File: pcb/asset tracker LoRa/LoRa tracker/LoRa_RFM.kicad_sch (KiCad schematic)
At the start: 2 parts

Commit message: pcb kastje
pcb in kastje getekend
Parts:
- removed MOD1: rfm95, Module:RFM69HW, symbol modulles:rfm95
- added C25: 10uF, vanalles:0603, symbol Device:C_Small
- added C26: 1uF, vanalles:0603, symbol Device:C_Small
- added C27: 0.1uF, vanalles:0603, symbol Device:C_Small
- added C32: 100nF, vanalles:0603, symbol Device:C_Small
- added CON3: jtag, connectors_user:Tag-Connect_TC2050-IDC-FP_2x05_P1.27mm_Vertical, symbol conectors:jtag
- added R9: 10K, vanalles:0603RL, symbol Device:R_Small_US
- added U8: murattaLora, Module:XCVR_CMWX1ZZABZ-078, symbol modulles:murattaLora
- R7: footprint vanalles:0603 -> vanalles:0603RL
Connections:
- net +3V3: now also C25.1, C26.1, C27.1, CON3.1 (VCC), R9.1, U8.32 (VREF+), U8.5 (VDD_MCU), U8.6 (VDD_RF); no longer R7.1
- net GND: now also R7.1, C25.2, C26.2, C27.2, C32.2, CON3.3 (GND), CON3.5 (GND), CON3.9 (GND), U8.25 (GND), U8.27 (GND), U8.3 (GND), U8.44 (GND), U8.49 (GND), U8.50 (GND), U8.51 (GND), U8.52 (GND), U8.53 (GND), U8.54 (GND), U8.55 (GND), U8.56 (GND), U8.57 (GND), U8.7 (GND)
- net CS_RFM: no longer names the net of R7.2
- net CS_RFM: now also U8.43 (BOOT0)
- new net ANT: U8.26 (ANT)
- new net CLK: U8.16 (PB13/SPI2_SCK)
- new net CS: U8.17 (PB12/SPI2_NSS)
- new net MISO: U8.15 (PB14/SPI2_MISO)
- new net MOSI: U8.14 (PB15/SPI2_MOSI)
- new net RESET: C32.1, CON3.10 (tRST), R9.2, U8.34 (MCU_NRST)
- new net SWCLK: CON3.4 (SWDCLK/TCK), U8.42 (PA14/SWCLK)
- new net SWDIO: CON3.2 (SWDIO/TMS), U8.41 (PA13/SWDIO)

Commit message: klaar
print hertekend naar stm32L5
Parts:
- added R10: 10K, vanalles:0603RL, symbol Device:R_Small_US
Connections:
- net +3V3: now also R10.1
- net CS: now also R10.2
- no-connect marks 5 -> 32
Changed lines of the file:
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@@
   (junction (at 171.45 33.02) (diameter 0.9144) (color 0 0 0 0))
   (junction (at 171.45 35.56) (diameter 0.9144) (color 0 0 0 0))
+  (junction (at 172.72 73.66) (diameter 0.9144) (color 0 0 0 0))
   (junction (at 189.23 31.75) (diameter 0.9144) (color 0 0 0 0))
   (junction (at 198.12 135.89) (diameter 0.9144) (color 0 0 0 0))
@@
   (junction (at 270.51 135.89) (diameter 0.9144) (color 0 0 0 0))
   (no_connect (at 100.33 33.02))
+  (no_connect (at 100.33 43.18))
+  (no_connect (at 100.33 45.72))
+  (no_connect (at 100.33 48.26))
+  (no_connect (at 100.33 50.8))
+  (no_connect (at 100.33 53.34))
+  (no_connect (at 100.33 55.88))
+  (no_connect (at 100.33 60.96))
+  (no_connect (at 100.33 63.5))
+  (no_connect (at 100.33 66.04))
+  (no_connect (at 100.33 68.58))
+  (no_connect (at 100.33 71.12))
+  (no_connect (at 100.33 73.66))
+  (no_connect (at 100.33 76.2))
+  (no_connect (at 100.33 78.74))
+  (no_connect (at 100.33 81.28))
+  (no_connect (at 100.33 83.82))
+  (no_connect (at 100.33 99.06))
+  (no_connect (at 100.33 101.6))
+  (no_connect (at 100.33 104.14))
+  (no_connect (at 100.33 109.22))
+  (no_connect (at 100.33 111.76))
   (no_connect (at 156.21 30.48))
   (no_connect (at 156.21 40.64))
+  (no_connect (at 156.21 58.42))
+  (no_connect (at 156.21 60.96))
+  (no_connect (at 156.21 63.5))
+  (no_connect (at 156.21 66.04))
+  (no_connect (at 156.21 68.58))
+  (no_connect (at 156.21 72.39))
   (no_connect (at 228.6 130.81))
   (no_connect (at 228.6 133.35))
@@
     (stroke (width 0) (type solid) (color 0 0 0 0))
   )
-  (wire (pts (xy 156.21 76.2) (xy 172.72 76.2))
-    (stroke (width 0) (type solid) (color 0 0 0 0))
-  )
-  (wire (pts (xy 156.21 78.74) (xy 172.72 78.74))
-    (stroke (width 0) (type solid) (color 0 0 0 0))
-  )
-  (wire (pts (xy 156.21 81.28) (xy 172.72 81.28))
+  (wire (pts (xy 156.21 76.2) (xy 191.77 76.2))
+    (stroke (width 0) (type solid) (color 0 0 0 0))
+  )
+  (wire (pts (xy 156.21 78.74) (xy 191.77 78.74))
+    (stroke (width 0) (type solid) (color 0 0 0 0))
+  )
+  (wire (pts (xy 156.21 81.28) (xy 191.77 81.28))
     (stroke (width 0) (type solid) (color 0 0 0 0))
   )
@@
   )
   (wire (pts (xy 171.45 35.56) (xy 171.45 38.1))
+    (stroke (width 0) (type solid) (color 0 0 0 0))
+  )
+  (wire (pts (xy 172.72 55.88) (xy 172.72 62.23))
+    (stroke (width 0) (type solid) (color 0 0 0 0))
+  )
+  (wire (pts (xy 172.72 67.31) (xy 172.72 73.66))
+    (stroke (width 0) (type solid) (color 0 0 0 0))
+  )
+  (wire (pts (xy 172.72 73.66) (xy 191.77 73.66))
     (stroke (width 0) (type solid) (color 0 0 0 0))
   )
@@
     (effects (font (size 1.27 1.27)) (justify right))
   )
-  (hierarchical_label "CS" (shape input) (at 172.72 73.66 0)
-    (effects (font (size 1.27 1.27)) (justify left))
-  )
-  (hierarchical_label "CLK" (shape input) (at 172.72 76.2 0)
-    (effects (font (size 1.27 1.27)) (justify left))
-  )
-  (hierarchical_label "MISO" (shape output) (at 172.72 78.74 0)
-    (effects (font (size 1.27 1.27)) (justify left))
-  )
-  (hierarchical_label "MOSI" (shape input) (at 172.72 81.28 0)
+  (hierarchical_label "CS" (shape input) (at 191.77 73.66 0)
+    (effects (font (size 1.27 1.27)) (justify left))
+  )
+  (hierarchical_label "CLK" (shape input) (at 191.77 76.2 0)
+    (effects (font (size 1.27 1.27)) (justify left))
+  )
+  (hierarchical_label "MISO" (shape output) (at 191.77 78.74 0)
+    (effects (font (size 1.27 1.27)) (justify left))
+  )
+  (hierarchical_label "MOSI" (shape input) (at 191.77 81.28 0)
     (effects (font (size 1.27 1.27)) (justify left))
   )
@@
     )
     (property "Datasheet" "" (id 3) (at 171.45 25.4 0)
+      (effects (font (size 1.27 1.27)) hide)
+    )
+    (pin "1")
+  )
+  (symbol (lib_id "power:+3V3") (at 172.72 55.88 0) (unit 1)
+    (in_bom yes) (on_board yes) (fields_autoplaced)
+    (property "Reference" "#PWR0161" (id 0) (at 172.72 59.69 0)
+      (effects (font (size 1.27 1.27)) hide)
+    )
+    (property "Value" "+3V3" (id 1) (at 172.72 52.07 0))
+    (property "Footprint" "" (id 2) (at 172.72 55.88 0)
+      (effects (font (size 1.27 1.27)) hide)
+    )
+    (property "Datasheet" "" (id 3) (at 172.72 55.88 0)
       (effects (font (size 1.27 1.27)) hide)
     )
@@
       (effects (font (size 1.27 1.27)) hide)
     )
+    (pin "1")
+    (pin "2")
+  )
+  (symbol (lib_id "Device:R_Small_US") (at 172.72 64.77 0) (unit 1)
+    (in_bom yes) (on_board yes) (fields_autoplaced)
+    (property "Reference" "R10" (id 0) (at 175.26 64.1349 0)
+      (effects (font (size 1.27 1.27)) (justify left))
+    )
+    (property "Value" "10K" (id 1) (at 175.26 66.6749 0)
+      (effects (font (size 1.27 1.27)) (justify left))
+    )
+    (property "Footprint" "vanalles:0603RL" (id 2) (at 172.72 64.77 0)
+      (effects (font (size 1.27 1.27)) hide)
+    )
+    (property "Datasheet" "~" (id 3) (at 172.72 64.77 0)
+      (effects (font (size 1.27 1.27)) hide)
+    )

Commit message: remake
remake 2 van de print
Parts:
- removed C32: 100nF, vanalles:0603, symbol Device:C_Small
- removed CON3: jtag, connectors_user:Tag-Connect_TC2050-IDC-FP_2x05_P1.27mm_Vertical, symbol conectors:jtag
- removed R10, R9: 10K, vanalles:0603RL, symbol Device:R_Small_US
- removed U8: murattaLora, Module:XCVR_CMWX1ZZABZ-078, symbol modulles:murattaLora
- added MOD1: RFM98W-433S2, Module:XCVR_RFM98W-433S2, symbol RFM98W-433S2:RFM98W-433S2
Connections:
- net +3V3: now also R7.1, MOD1.13 (3.3V), MOD1.13_1 (3.3V)
- net ANT: now also MOD1.9 (ANT), MOD1.9_1 (ANT)
- net CLK: now also MOD1.4 (SCK), MOD1.4_1 (SCK)
- net CS: now also R7.2, MOD1.5 (NSS), MOD1.5_1 (NSS)
- net GND: now also MOD1.1 (GND), MOD1.10 (GND), MOD1.10_1 (GND), MOD1.1_1 (GND), MOD1.8 (GND), MOD1.8_1 (GND); no longer R7.1
- net MISO: now also MOD1.2 (MISO), MOD1.2_1 (MISO)
- net MOSI: now also MOD1.3 (MOSI), MOD1.3_1 (MOSI)
- net RESET: now also MOD1.6 (RESET), MOD1.6_1 (RESET)
- new net: MOD1.11 (DIO3), MOD1.11_1 (DIO3)
- new net: MOD1.12 (DIO4), MOD1.12_1 (DIO4)
- new net: MOD1.14 (DIO0), MOD1.14_1 (DIO0)
- new net: MOD1.15 (DIO1), MOD1.15_1 (DIO1)
- new net: MOD1.16 (DIO2), MOD1.16_1 (DIO2)
- new net: MOD1.7 (DIO5), MOD1.7_1 (DIO5)
- no-connect marks 32 -> 6

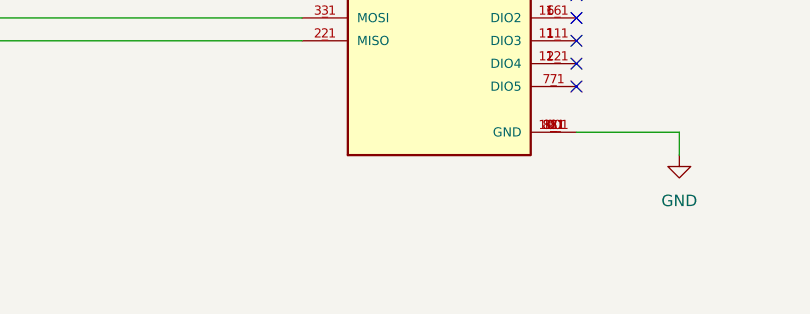
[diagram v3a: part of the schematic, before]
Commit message: versie2
aan versie 2 begonnen met tekenen en code beginnen schrijven voor quadkey
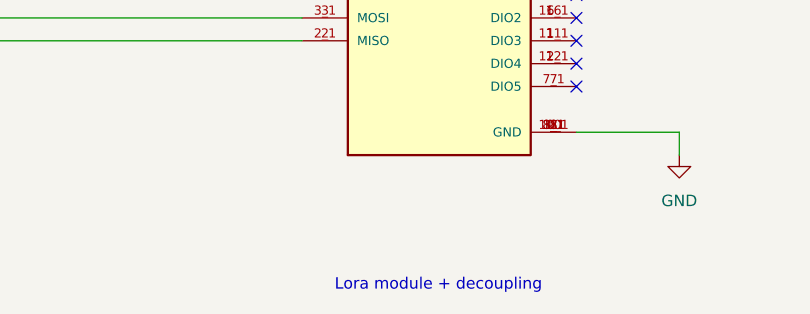
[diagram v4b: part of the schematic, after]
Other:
- note added: "Lora module + decoupling"
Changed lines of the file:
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@@
     (stroke (width 0) (type solid) (color 0 0 0 0))
+  )
+  (text "Lora module + decoupling" (at 134.62 104.14 180)
+    (effects (font (size 1.27 1.27)) (justify right bottom))
   )
   (hierarchical_label "RESET" (shape input) (at 72.39 63.5 180)
